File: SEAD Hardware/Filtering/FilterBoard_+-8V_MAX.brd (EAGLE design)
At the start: 98 x 80 mm, 98 parts, among them U1 TLC2272A_D_8, U2 TLC2272A_D_8, U3 TLC2272A_D_8, U4 TLC2272A_D_8, U5 TLC2272A_D_8, U6 TLC2272A_D_8, U7 TPS7A3301_RGW_20, U8 TPS84250_RKG_41

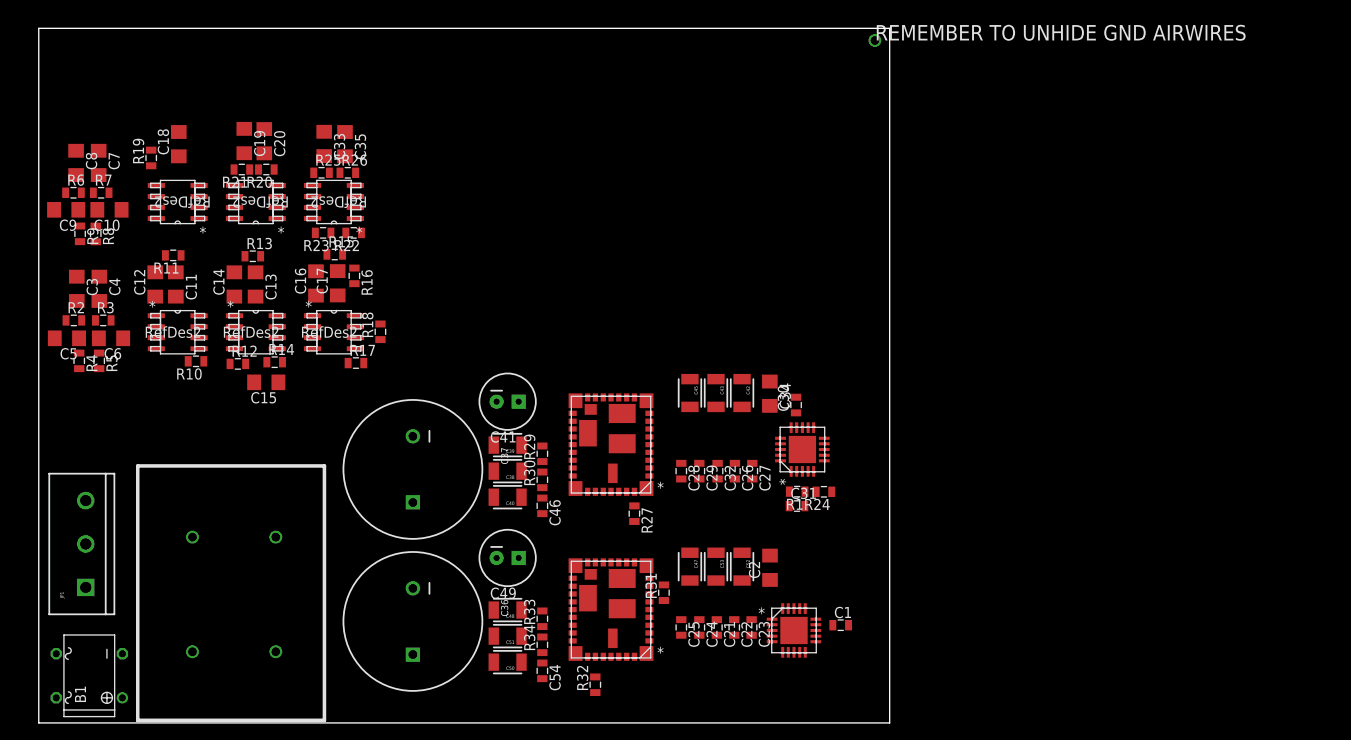
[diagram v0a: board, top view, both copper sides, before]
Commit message: Finished new filter board prototype.
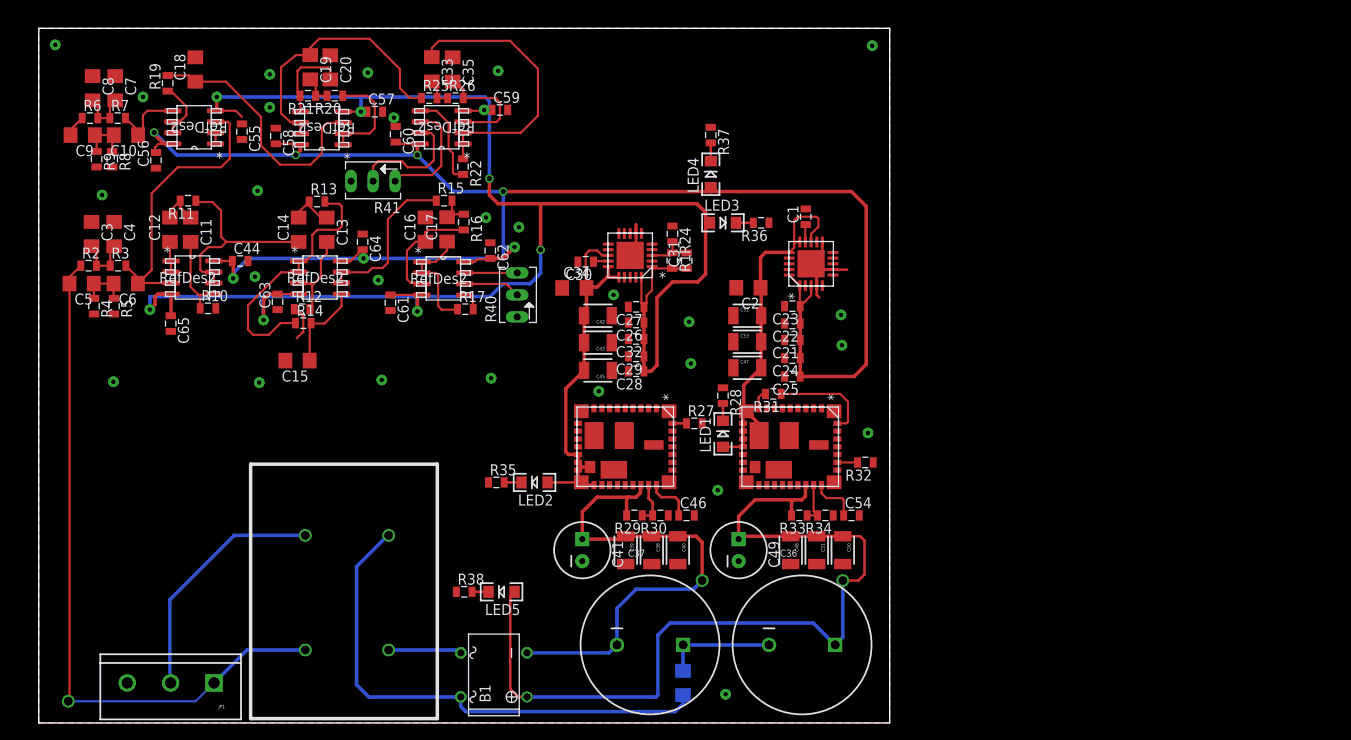
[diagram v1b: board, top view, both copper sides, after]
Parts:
- removed R18, R23: (no value), SensorCape:0805
- added C44, C55, C56, C57, C58, C59, C60, C61, C62, C63, C64, C65: 10nF, SensorCape:0805
- added LED1, LED2, LED3, LED4, LED5: (no value), ASL:LED-1206
- added R28, R35, R36, R37, R38: (no value), ASL:0805
- added R39: 0, ASL:1206
- added R40, R41: (no value), pot:B64Y
- moved C1 47.2 mm to (88.3, 58.3), turned to 90 degrees
- moved B1 46.6 mm to (52.4, 5.53)
- moved C36 44.9 mm to (87.9, 8.99), turned to 0 degrees
- moved U$2 42.3 mm to (89.0, 52.9), turned to 90 degrees
- moved C50 40.7 mm to (92.6, 19.9), turned to 270 degrees
- moved R32 40.3 mm to (95.2, 30.0), turned to 180 degrees
- moved C54 39.8 mm to (93.6, 23.9), turned to 0 degrees
- moved C23 37.3 mm to (86.8, 48.0), turned to 180 degrees
- moved C51 37.0 mm to (89.6, 19.9), turned to 270 degrees
- moved R34 35.8 mm to (90.6, 23.9), turned to 180 degrees
- moved C22 35.6 mm to (86.8, 46.0), turned to 180 degrees
- moved U8 35.3 mm to (91.6, 35.9), turned to 270 degrees
- moved R24 34.5 mm to (73.0, 56.3), turned to 270 degrees
- moved C21 34.2 mm to (86.8, 44.1), turned to 180 degrees
- moved C37 34.0 mm to (70.4, 8.99), turned to 0 degrees
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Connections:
- removed net HVSS_8D: U1.4, U2.4, U3.4, U4.4, U5.4, U6.4
- new net N$30: LED1.C, R28.2
- new net N$45: LED2.C, R35.2
- new net N$46: LED3.C, R36.2
- new net N$47: LED4.C, R37.2
- new net N$48: LED5.C, R38.2
- new net VDD_L_CHOKE: B1.AC2, R39.1
- net GND: now also C44.2, C55.2, C56.1, C57.2, C58.1, C59.2, C60.1, C61.2, C62.1, C63.1, C64.1, C65.2, R28.1, R35.1, R36.1, R37.1, R38.1, R39.2; no longer B1.AC2
- net HVDD_15D: now also LED1.A
- net HVDD_8A: now also C44.1, C56.2, C58.2, C60.2, C62.2, C64.2, LED4.A
- net HVDD_IN: now also LED5.A
- net HVSS_15D: now also LED2.A
- net HVSS_8A: now also C55.1, C57.1, C59.1, C61.1, C63.2, C65.1, LED3.A, U1.4, U2.4, U3.4, U4.4, U5.4, U6.4
- net N$19: now also R40.S; no longer R18.1
- net N$22: now also R41.E; no longer R23.1
- net OUT_15KHZ: now also R41.S; no longer R23.2
- net OUT_15_100_KHZ: now also R40.A; no longer R18.2
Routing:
- net HVSS_8A: track 0.00 -> 206.2 mm, vias 0 -> 8
- net HVDD_8A: track 0.00 -> 196.6 mm, vias 0 -> 7
- net HVDD_IN: track 0.00 -> 101.6 mm, vias 0 -> 1
- net VDD_IN: track 0.00 -> 80.5 mm, vias 1 -> 2
- net VDD_L_CHOKE: track 0.00 -> 59.7 mm, vias 0 -> 1
- net HVSS_IN: track 0.00 -> 58.5 mm, vias 0 -> 1
- net HVDD_15D: track 0.00 -> 46.8 mm
- net HVSS_15D: track 0.00 -> 45.0 mm
- net N$7: track 0.00 -> 33.9 mm
- net N$4: track 0.00 -> 32.8 mm
- net N$24: track 0.00 -> 31.3 mm
- net GND: track 0.00 -> 30.9 mm, vias 2 -> 27
- net N$16: track 0.00 -> 30.2 mm
- net N$29: track 0.00 -> 30.1 mm
- net VDD_L: track 0.00 -> 28.3 mm
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- added copper zone on layer 1, net GND
- added copper zone on layer 16, net GND
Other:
- board text removed: "REMEMBER TO UNHIDE GND AIRWIRES"

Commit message: Fixed -V switcher on filtering board.
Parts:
- removed C44, C55, C56, C57, C62, C63: 10nF, SensorCape:0805
- removed R40, R41: (no value), pot:B64Y
- removed U1, U2, U3, U4, U5, U6: TLC2272A_D_8, SensorCape:D8
- added IC1, IC2, IC3: TL084D, linear:SO14
- added R18, R23: (no value), pot:SP19L
- moved R15 44.7 mm to (7.30, 39.0), turned to 180 degrees
- moved R17 41.8 mm to (11.0, 64.8), turned to 180 degrees
- moved C3 41.7 mm to (8.52, 14.7), turned to 0 degrees
- moved C64 41.1 mm to (4.97, 30.1), turned to 0 degrees
- moved C4 39.0 mm to (8.52, 17.3), turned to 0 degrees
- moved R2 38.8 mm to (12.2, 14.4), turned to 90 degrees
- moved C5 38.2 mm to (14.2, 13.6), turned to 270 degrees
- moved C61 36.6 mm to (5.33, 58.7), turned to 180 degrees
- moved R3 35.0 mm to (12.2, 17.8), turned to 90 degrees
- moved R4 34.6 mm to (16.8, 15.0), turned to 0 degrees
- moved R11 33.7 mm to (16.1, 26.5), turned to 0 degrees
- moved C12 32.9 mm to (10.1, 24.3), turned to 0 degrees
- moved C11 32.6 mm to (15.2, 24.3), turned to 180 degrees
- moved C6 32.2 mm to (14.2, 18.6), turned to 270 degrees
- moved R5 31.8 mm to (16.8, 17.3), turned to 0 degrees
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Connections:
- removed net N$11: U4.1, U4.2
- net GND: now also U$2.6, U$2.9; no longer C44.2, C55.2, C56.1, C57.2, C62.1, C63.1, U$1.1, U$1.32, U$1.33, U$1.34, U$1.37, U$1.4, U$1.5, U$1.8, U$1.9
- net HVDD_8A: now also IC1.4, IC2.4, IC3.4; no longer C44.1, C56.2, C62.2, U1.8, U2.8, U3.8, U4.8, U5.8, U6.8
- net HVSS_15D: now also U$1.1, U$1.32, U$1.33, U$1.34, U$1.37, U$1.4, U$1.5, U$1.8, U$1.9
- net HVSS_8A: now also IC1.11, IC2.11, IC3.11; no longer C55.1, C57.1, C63.2, U1.4, U2.4, U3.4, U4.4, U5.4, U6.4
- net N$10: now also IC2.12; no longer U4.5
- net N$12: now also IC1.1, IC1.2; no longer U1.1, U1.2
- net N$14: now also IC1.5; no longer U1.5
- net N$15: now also IC1.6, IC1.7; no longer U1.6, U1.7
- net N$16: now also IC1.8, IC1.9; no longer U2.1, U2.2
- net N$17: now also IC1.13, IC1.14; no longer U2.6, U2.7
- net N$18: now also IC2.1, IC2.2; no longer U3.1, U3.2
- net N$19: now also IC2.6, R18.S; no longer R40.S, U3.6
- net N$20: now also IC3.10; no longer U6.3
- net N$21: now also IC3.12; no longer U6.5
- net N$22: now also IC3.13, R23.S; no longer R41.E, U6.6
- net N$24: now also IC3.6, IC3.7; no longer U5.6, U5.7
- net N$26: now also IC3.5; no longer U5.5
- net N$28: now also IC3.1, IC3.2; no longer U5.1, U5.2
- net N$29: now also IC3.3; no longer U5.3
- net N$3: now also IC2.8, IC2.9
- net N$31: now also IC2.13, IC2.14; no longer U4.6, U4.7
- net N$36: now also IC1.10; no longer U2.3
- net N$38: now also IC1.12; no longer U2.5
- net N$4: now also IC3.8, IC3.9; no longer U6.1, U6.2
- net N$41: now also IC2.3; no longer U3.3
- net N$42: now also IC2.5; no longer U3.5
- net N$7: now also IC1.3, IC2.10; no longer U1.3, U4.3
- net OUT_15KHZ: now also IC3.14, R23.E; no longer R41.S, U6.7
- net OUT_15_100_KHZ: now also IC2.7, R18.E; no longer R40.A, U3.7
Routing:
- net N$40: track 4.21 -> 64.5 mm
- net VDD_IN: track 80.5 -> 28.4 mm
- net OUT_15KHZ: track 14.1 -> 40.8 mm, vias 0 -> 1
- net N$16: track 30.2 -> 5.07 mm
- net N$23: track 3.39 -> 26.6 mm
- net HVSS_15D: track 45.0 -> 68.0 mm
- net N$7: track 33.9 -> 54.0 mm, vias 0 -> 2
- net N$4: track 32.8 -> 14.6 mm
- net N$9: track 6.15 -> 23.9 mm
- net N$22: track 13.1 -> 30.6 mm
- net N$15: track 23.8 -> 6.88 mm
- net N$24: track 31.3 -> 16.2 mm
- net N$17: track 18.6 -> 6.31 mm
- net N$29: track 30.1 -> 18.7 mm
- net N$38: track 10.1 -> 21.4 mm
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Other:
- board text added: "(c) 2014 Pavlo Manovi pavlo.me"
- board text added: "40V Pk-Pk AC Input Abs. Max!"
- board text added: "SEAD Filtering Board v1.5"

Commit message: Filtering Circuit v1.6
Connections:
- net GND: no longer C46.2, U$1.30
- net HVSS_15D: now also C46.2, U$1.29, U$1.30
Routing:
- net HVSS_15D: track 68.0 -> 82.7 mm
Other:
- board text added: "SEAD Filtering Board v1.6"
- board text removed: "SEAD Filtering Board v1.5"
